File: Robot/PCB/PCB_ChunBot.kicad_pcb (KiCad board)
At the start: 2 copper layers, 132.9 x 139 mm, 63 parts, among them J1 HC-SR04, J10 Servo1, J11 Servo2, J12 Servo3, J13 NRF24L01, J14 ServoR, J15 Sensor central-R, J2 Servo4, J3 Servo5, J4 Barrel_Jack_Switch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

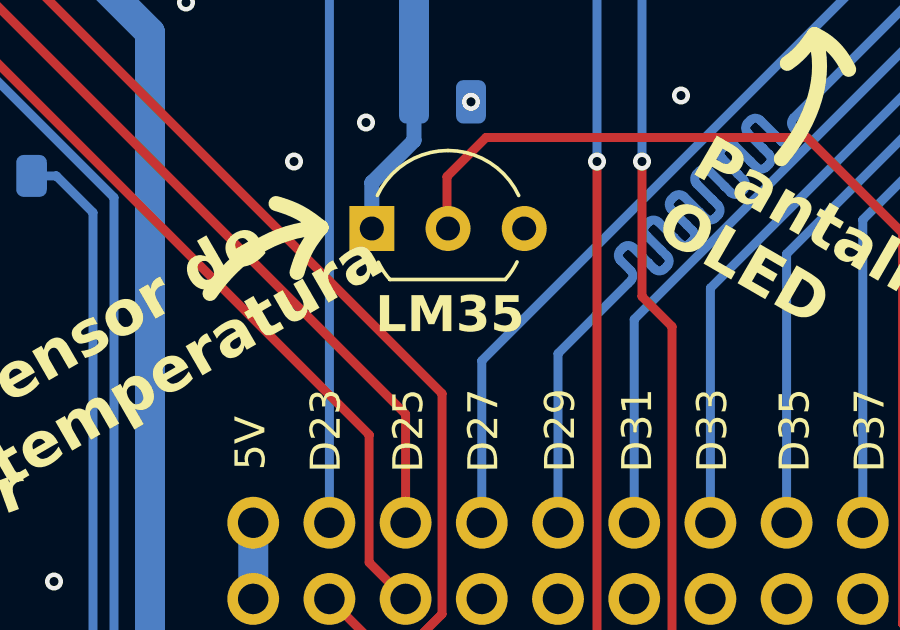
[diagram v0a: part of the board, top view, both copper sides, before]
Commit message: [Modified] Cambio serigrafia para soporte de sensor de temperatura TMP36
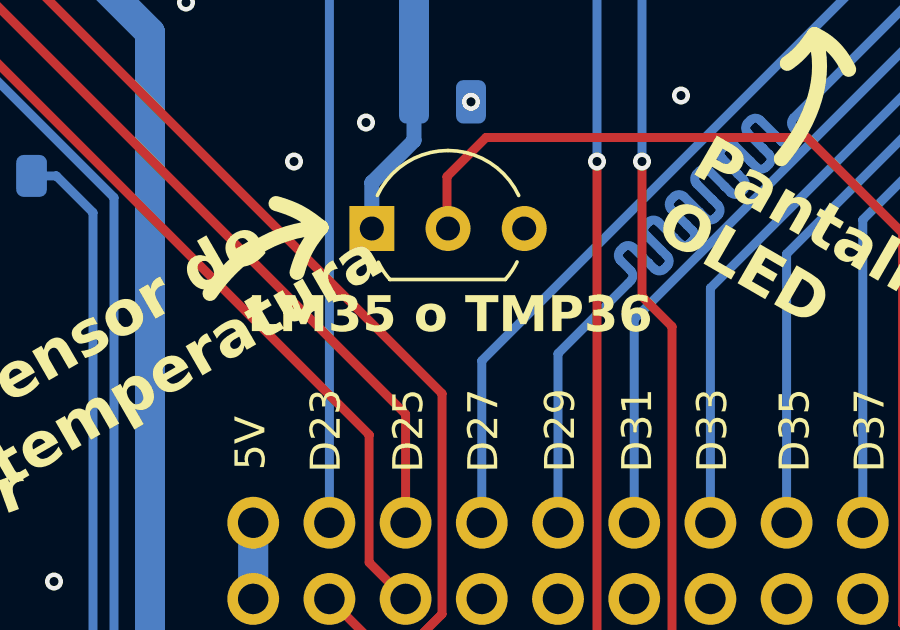
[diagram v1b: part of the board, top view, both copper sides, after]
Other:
- board text added: "LM35 o TMP36"
- board text removed: "LM35"
